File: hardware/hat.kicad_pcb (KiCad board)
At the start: 4 copper layers, 65 x 56.6 mm, 144 parts, among them J101 Raspberry_Pi_2_3, J102 Boot, J201 USB Power In, K201 CONN_3, P101 Debug, P201 Black, P301 CON-SENSOR2, P302 CON-SENSOR2, P303 CON-SENSOR2, P304 CON-SENSOR2, P305 CON-SENSOR2, P306 CON-SENSOR2, P307 CON-SENSOR2, P308 CON-SENSOR2, Q101 2N7002P, Q102 2N7002P, Q103 NTR2101P, Q104 NTR2101P, U101 XMC1404, U102 LD1117, U201 MAX17260_LS, U202 BQ2407X, U203 AOZ1212, U204 MIC2253, U205 AP7333-33SAG-7, U301 74AHC244, U302 74AHC244, U303 74AHC244, U304 74AHC244, X101 16MHz, X102 32.768kHz

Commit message: thermal improvement
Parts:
- moved R209 4.03 mm to (187.1, 70.0), turned to 270 degrees
- moved R210 3.86 mm to (184.4, 70.0), turned to 270 degrees
- moved R208 2.56 mm to (188.4, 71.6), turned to 270 degrees
- moved R219 0.71 mm to (185.8, 70.0)
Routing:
- net GND: track 368.8 -> 372.0 mm, vias 322 -> 331
- net CHG-nCHG: track 66.2 -> 67.4 mm
- net CHG-nPGOOD: track 69.6 -> 70.5 mm
- net Net-(R209-Pad2): track 2.27 -> 3.13 mm
- net CHG-EN1: track 63.5 -> 64.0 mm
- added copper zone on F.Cu, net BOOST-OUT

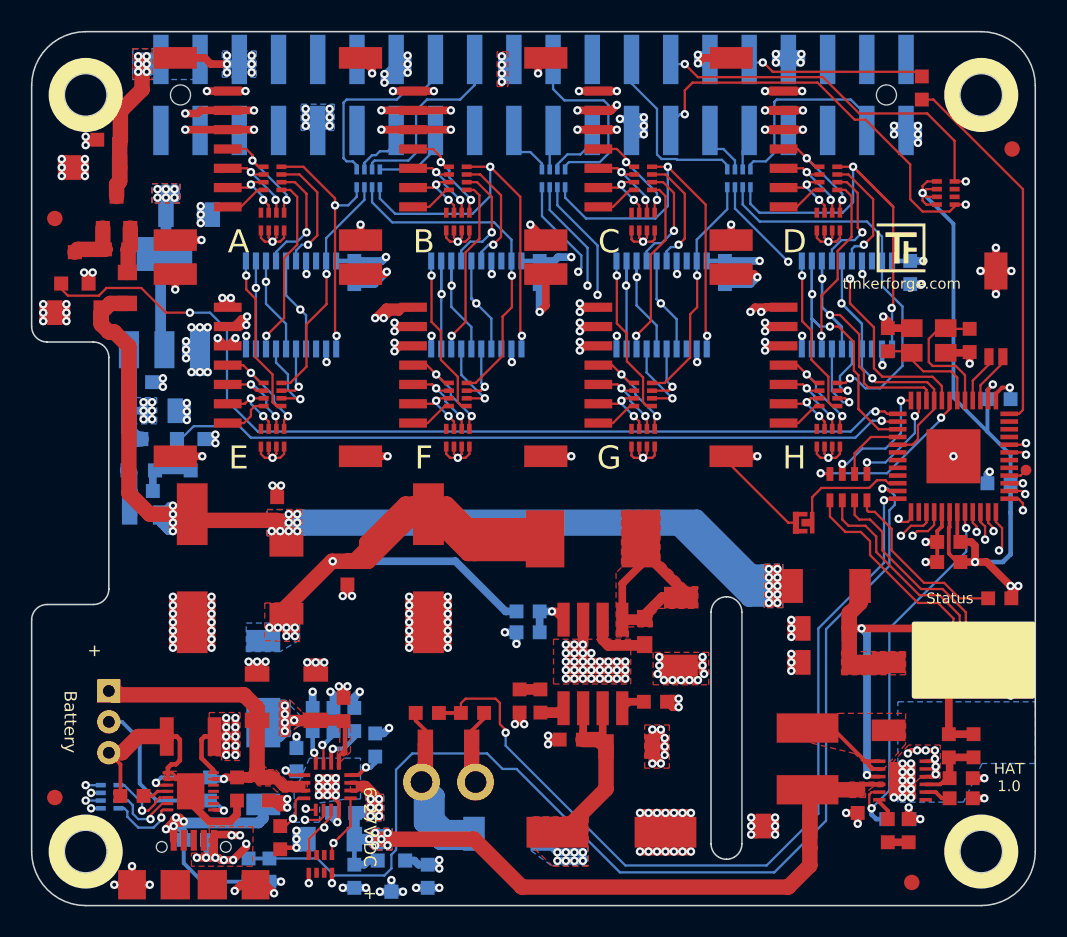
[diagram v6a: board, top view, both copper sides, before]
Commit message: completely routed, optimzations missing.
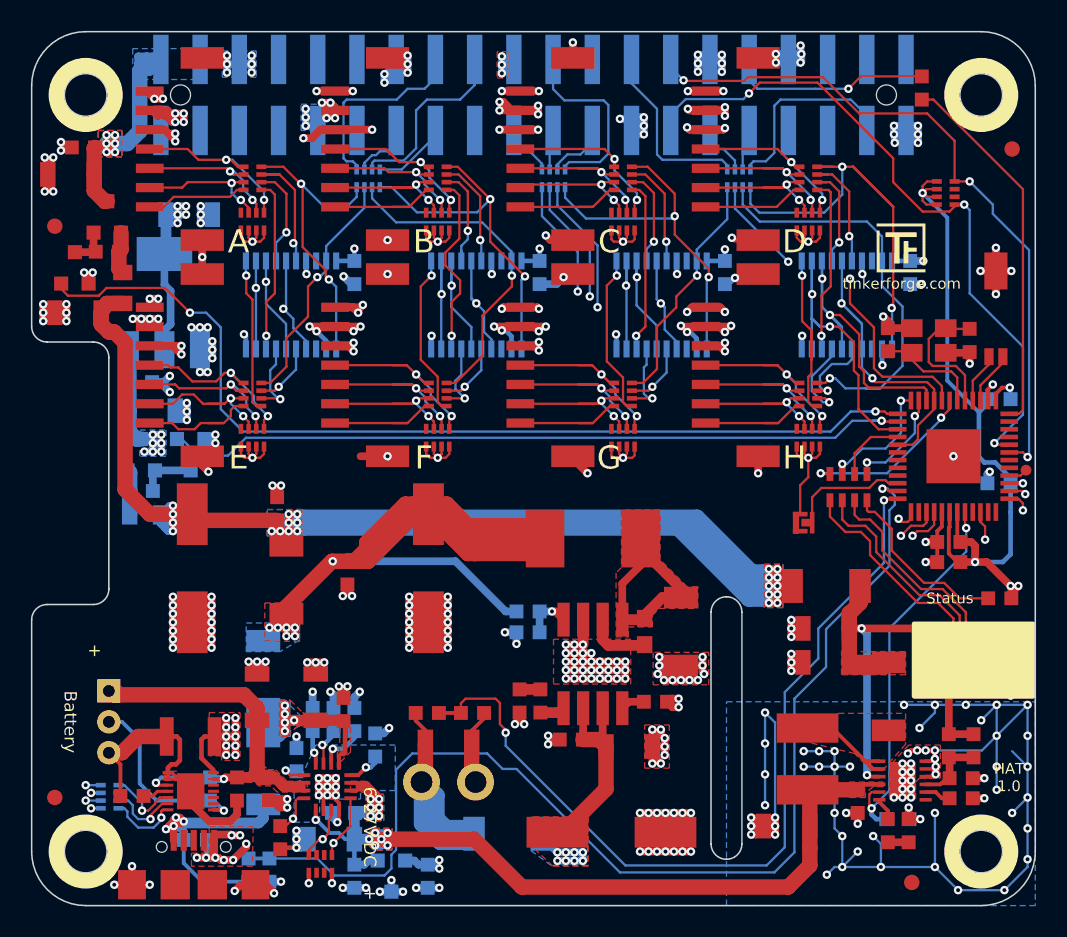
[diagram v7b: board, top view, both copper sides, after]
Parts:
- moved P301 4.55 mm to (178.7, 33.0), turned to 90 degrees
- moved P302 4.55 mm to (178.7, 47.0), turned to 90 degrees
- moved P303 4.55 mm to (190.7, 33.0), turned to 90 degrees
- moved P304 4.55 mm to (190.7, 47.0), turned to 90 degrees
- moved P305 4.55 mm to (202.7, 33.0), turned to 90 degrees
- moved P306 4.55 mm to (202.7, 47.0), turned to 90 degrees
- moved P307 4.55 mm to (214.7, 33.0), turned to 90 degrees
- moved P308 4.55 mm to (214.7, 47.0), turned to 90 degrees
- moved C111 1.72 mm to (169.6, 32.9)
- moved C110 1.71 mm to (168.8, 34.6)
- moved CP301 1.30 mm to (180.5, 37.7)
- moved CP302 1.30 mm to (180.5, 51.7)
- moved CP303 1.30 mm to (192.5, 37.7)
- moved CP304 1.30 mm to (192.5, 51.7)
- moved CP305 1.30 mm to (204.5, 37.7)
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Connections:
- J101 pad 27: RASP-SC -> RASP-SD
- J101 pad 28: RASP-SD -> RASP-SC
- R219 pad 1: CHG-SYSOFF -> Net-(R219-Pad1)
- RP101 pad 5: RASP-SC -> RASP-SD
- RP101 pad 8: RASP-SD -> RASP-SC
- U101 pad 21: CHG-SYSOFF -> (no net)
- U101 pad 23: CHG-EN2 -> (no net)
- U101 pad 24: CHG-EN1 -> (no net)
- U202 pad 15: CHG-SYSOFF -> Net-(R219-Pad1)
- U202 pad 5: CHG-EN2 -> BOOST-IN
- U202 pad 6: CHG-EN1 -> GND
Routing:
- net B-5V: track 130.7 -> 28.6 mm, vias 22 -> 23
- net B-3V3: track 186.1 -> 97.1 mm, vias 26 -> 25
- net GND: track 372.0 -> 449.2 mm, vias 331 -> 379
- net CHG-EN1: track 64.0 -> 0.00 mm, vias 2 -> 0
- net CHG-EN2: track 61.7 -> 0.00 mm, vias 2 -> 0
- net CHG-SYSOFF: track 58.8 -> 0.00 mm, vias 2 -> 0
- net RASP-PWR: track 15.7 -> 22.0 mm
- net Net-(CP302-Pad3): track 4.92 -> 10.3 mm
- net Net-(CP303-Pad3): track 4.77 -> 10.1 mm
- net Net-(CP308-Pad3): track 4.67 -> 9.82 mm
- net Net-(P302-Pad7): track 3.02 -> 8.15 mm
- net Net-(CP307-Pad3): track 4.77 -> 9.82 mm
- net Net-(CP306-Pad3): track 4.77 -> 9.82 mm
- net Net-(CP304-Pad3): track 4.77 -> 9.82 mm
- net Net-(CP308-Pad2): track 5.80 -> 10.8 mm
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- removed copper zone on B.Cu, net B-3V3
- removed copper zone on F.Cu, net B-3V3
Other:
- board text added: "OVP, Switch?"

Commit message: fix text positions
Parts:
- moved G*** 4.13 mm to (220.8, 33.7)
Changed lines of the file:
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@@
   (page A4)
   (layers
-    (0 F.Cu signal)
+    (0 F.Cu signal hide)
     (1 GND signal hide)
     (2 VCC signal hide)
-    (31 B.Cu signal)
+    (31 B.Cu signal hide)
     (32 B.Adhes user)
     (33 F.Adhes user hide)
@@
   )
   (setup
-    (last_trace_width 0.5)
+    (last_trace_width 0.15)
     (user_trace_width 0.15)
     (user_trace_width 0.2)
@@
     (aux_axis_origin 166.2 26)
     (grid_origin 166.2 26)
-    (visible_elements FFFDDF7F)
+    (visible_elements FFFCDF7F)
     (pcbplotparams
       (layerselection 0x00020_00000000)
@@
   )
   (module kicad-libraries:Logo_31x31 (layer F.Cu)
-    (at 220.925 37.825)
+    (at 220.8 33.7)
     (fp_text reference G*** (at 1.34874 2.97434) (layer F.SilkS) hide
       (effects (font (size 0.29972 0.29972) (thickness 0.0762)))
@@
     (effects (font (size 0.8 0.8) (thickness 0.15)))
   )
-  (gr_text tinkerforge.com (at 222.55 41.725) (layer F.SilkS)
+  (gr_text tinkerforge.com (at 222.4 37.65) (layer F.SilkS)
     (effects (font (size 0.7 0.7) (thickness 0.15)))
   )
@@
     (effects (font (size 0.7 0.7) (thickness 0.15)) (justify right))
   )
-  (gr_text "6-27V DC" (at 188.1 76.9 270) (layer F.SilkS)
+  (gr_text "6-27V DC" (at 187.9 76.9 270) (layer F.SilkS)
     (effects (font (size 0.8 0.8) (thickness 0.15)))
   )
@@
   (gr_arc (start 227.7 78.5) (end 231.2 78.5) (angle 90) (layer Edge.Cuts) (width 0.09906))
   (gr_arc (start 227.7 28.9) (end 227.7 25.4) (angle 90) (layer Edge.Cuts) (width 0.09906))
-  (gr_text D (at 215.6 39) (layer F.SilkS)
+  (gr_text D (at 215.7 27) (layer F.SilkS)
     (effects (font (size 1.5 1.5) (thickness 0.3)))
   )
-  (gr_text C (at 203.6 39) (layer F.SilkS)
+  (gr_text C (at 203.7 27) (layer F.SilkS)
     (effects (font (size 1.5 1.5) (thickness 0.3)))
   )
-  (gr_text H (at 215.6 53) (layer F.SilkS)
+  (gr_text H (at 215.7 41) (layer F.SilkS)
     (effects (font (size 1.5 1.5) (thickness 0.3)))
   )
-  (gr_text G (at 203.6 53) (layer F.SilkS)
+  (gr_text G (at 203.7 41) (layer F.SilkS)
     (effects (font (size 1.5 1.5) (thickness 0.3)))
   )
-  (gr_text F (at 191.6 53) (layer F.SilkS)
+  (gr_text F (at 191.7 41) (layer F.SilkS)
     (effects (font (size 1.5 1.5) (thickness 0.3)))
   )
-  (gr_text E (at 179.6 53) (layer F.SilkS)
+  (gr_text E (at 179.7 41) (layer F.SilkS)
     (effects (font (size 1.5 1.5) (thickness 0.3)))
   )
-  (gr_text B (at 191.6 39) (layer F.SilkS)
+  (gr_text B (at 191.7 27) (layer F.SilkS)
     (effects (font (size 1.5 1.5) (thickness 0.3)))
   )
-  (gr_text A (at 179.6 39) (layer F.SilkS)
+  (gr_text A (at 179.7 27) (layer F.SilkS)
     (effects (font (size 1.5 1.5) (thickness 0.3)))
   )
